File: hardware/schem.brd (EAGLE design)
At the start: 46 x 47 mm, 18 parts, among them IC1 7805L, IC2 L298

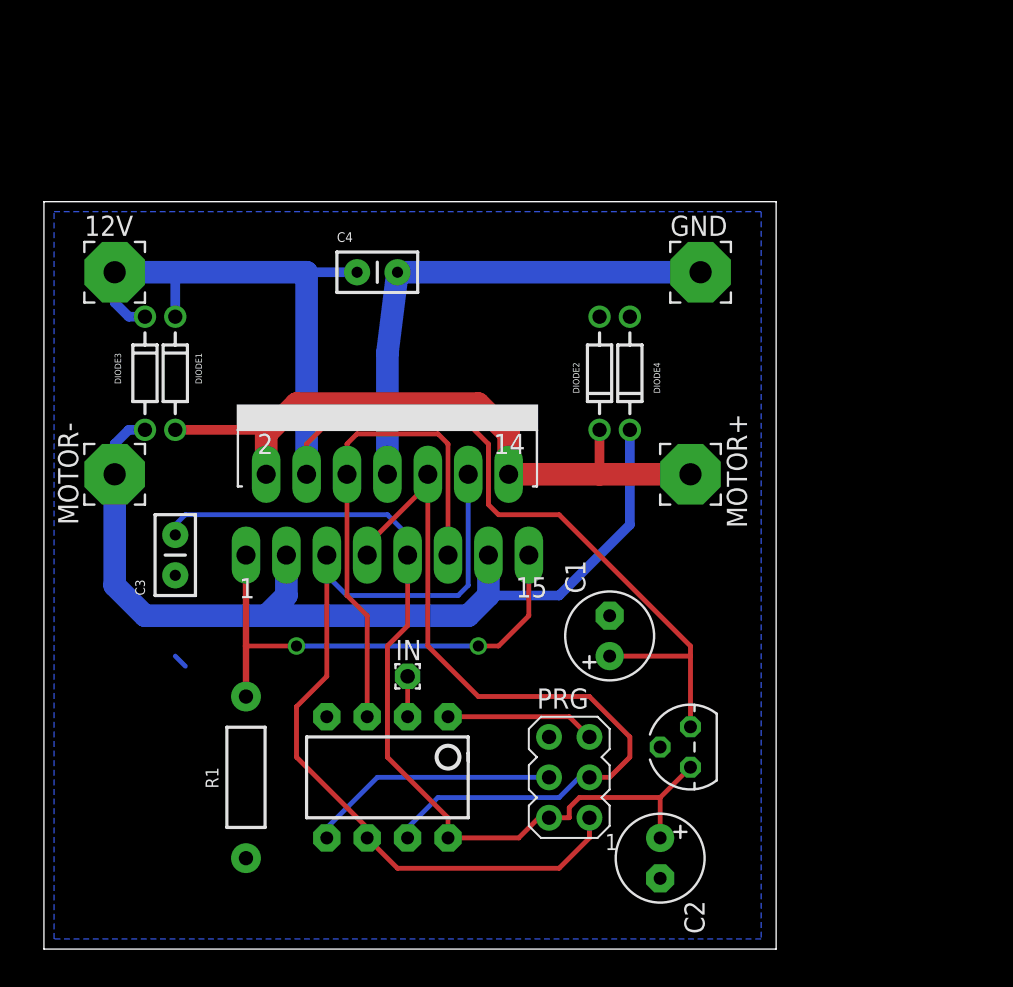
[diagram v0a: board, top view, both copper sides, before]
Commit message: added current sensing
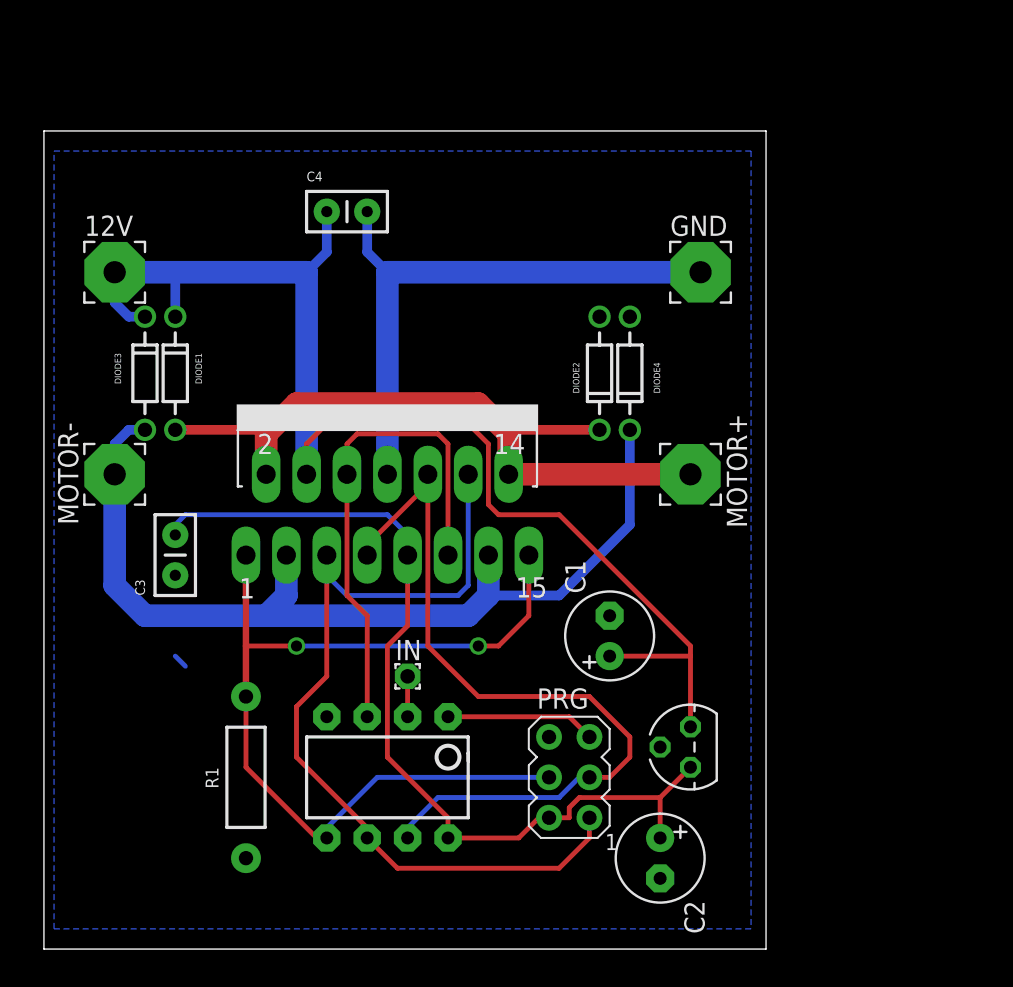
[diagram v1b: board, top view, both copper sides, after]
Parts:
- moved C4 4.26 mm to (17.8, 46.4)
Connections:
- removed net N$1: IC2.1, IC2.15, R1.P$1
- net MOSI: now also IC2.1, IC2.15, R1.P$1
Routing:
- net MOSI: track 15.9 -> 58.6 mm, vias 0 -> 2
- net N$1: track 31.3 -> 0.00 mm, vias 2 -> 0
- net GND: track 32.7 -> 37.6 mm
- net OUT1: track 42.3 -> 45.0 mm
- net +12V: track 79.7 -> 80.8 mm
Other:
- board size 46 x 47 mm -> 45.4 x 51.4 mm
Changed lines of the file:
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@@
 <board>
 <plain>
-<wire x1="0" y1="0" x2="46.025" y2="0" width="0" layer="20"/>
-<wire x1="46.025" y1="0" x2="46.025" y2="46.98" width="0" layer="20"/>
-<wire x1="46.025" y1="46.98" x2="0" y2="46.98" width="0" layer="20"/>
-<wire x1="0" y1="46.98" x2="0" y2="0" width="0" layer="20"/>
+<wire x1="0" y1="0" x2="45.39" y2="0" width="0" layer="20"/>
+<wire x1="45.39" y1="0" x2="45.39" y2="51.425" width="0" layer="20"/>
+<wire x1="45.39" y1="51.425" x2="0" y2="51.425" width="0" layer="20"/>
+<wire x1="0" y1="51.425" x2="0" y2="0" width="0" layer="20"/>
 </plain>
 <attributes>
@@
 </element>
 <element name="C3" library="SparkFun-Capacitors" package="CAP-PTH-SMALL2" value="100nF" x="8.255" y="23.495" rot="R90"/>
-<element name="C4" library="SparkFun-Capacitors" package="CAP-PTH-SMALL2" value="100nF" x="19.685" y="42.545"/>
+<element name="C4" library="SparkFun-Capacitors" package="CAP-PTH-SMALL2" value="100nF" x="17.78" y="46.355"/>
 <element name="R1" library="SparkFun-Passives" package="AXIAL-0.4" value="" x="12.7" y="10.795" smashed="yes" rot="R270">
 <attribute name="NAME" x="10.16" y="11.43" size="0.8128" layer="25" font="vector" ratio="15" rot="R270"/>
@@
 <wire x1="8.255" y1="42.545" x2="16.51" y2="42.545" width="1.4224" layer="16"/>
 <wire x1="16.51" y1="42.545" x2="16.51" y2="29.845" width="1.4224" layer="16"/>
-<wire x1="19.685" y1="42.545" x2="16.51" y2="42.545" width="0.6096" layer="16"/>
+<wire x1="17.78" y1="46.355" x2="17.78" y2="43.815" width="0.6096" layer="16"/>
+<wire x1="17.78" y1="43.815" x2="16.51" y2="42.545" width="0.6096" layer="16"/>
 <wire x1="32.385" y1="27.305" x2="28.575" y2="27.305" width="0.3048" layer="1"/>
 <wire x1="28.575" y1="27.305" x2="27.94" y2="27.94" width="0.3048" layer="1"/>
@@
 <contactref element="DIODE4" pad="P$2"/>
 <contactref element="DIODE2" pad="P$2"/>
-<wire x1="21.59" y1="29.845" x2="21.59" y2="37.465" width="1.4224" layer="16"/>
-<wire x1="21.59" y1="37.465" x2="22.225" y2="42.545" width="1.4224" layer="16"/>
-<wire x1="22.225" y1="42.545" x2="41.275" y2="42.545" width="1.4224" layer="16"/>
+<wire x1="21.59" y1="29.845" x2="21.59" y2="42.545" width="1.4224" layer="16"/>
+<wire x1="21.59" y1="42.545" x2="41.275" y2="42.545" width="1.4224" layer="16"/>
+<wire x1="20.32" y1="46.355" x2="20.32" y2="43.815" width="0.6096" layer="16"/>
+<wire x1="20.32" y1="43.815" x2="21.59" y2="42.545" width="0.6096" layer="16"/>
 <polygon width="0.3048" layer="16" isolate="0.6096">
-<vertex x="0.635" y="46.355"/>
-<vertex x="45.085" y="46.355"/>
-<vertex x="45.085" y="0.635"/>
-<vertex x="0.635" y="0.635"/>
+<vertex x="0.635" y="50.165"/>
+<vertex x="44.45" y="50.165"/>
+<vertex x="44.45" y="1.27"/>
+<vertex x="0.635" y="1.27"/>
 </polygon>
 <wire x1="8.255" y1="18.415" x2="8.89" y2="17.78" width="0.3048" layer="16"/>
@@
 <wire x1="20.955" y1="10.795" x2="17.78" y2="7.62" width="0.3048" layer="16"/>
 <wire x1="17.78" y1="7.62" x2="17.78" y2="6.985" width="0.3048" layer="16"/>
+<contactref element="IC2" pad="1"/>
+<contactref element="IC2" pad="15"/>
+<contactref element="R1" pad="P$1"/>
+<wire x1="12.7" y1="24.765" x2="12.7" y2="19.05" width="0.4064" layer="1"/>
+<wire x1="12.7" y1="19.05" x2="12.7" y2="15.875" width="0.4064" layer="1"/>
+<wire x1="30.48" y1="24.765" x2="30.48" y2="20.955" width="0.3048" layer="1"/>
+<wire x1="30.48" y1="20.955" x2="28.575" y2="19.05" width="0.3048" layer="1"/>
+<via x="27.305" y="19.05" extent="1-16" drill="0.7"/>
+<wire x1="27.305" y1="19.05" x2="15.875" y2="19.05" width="0.3048" layer="16"/>
+<via x="15.875" y="19.05" extent="1-16" drill="0.7"/>
+<wire x1="15.875" y1="19.05" x2="12.7" y2="19.05" width="0.3048" layer="1"/>
+<wire x1="28.575" y1="19.05" x2="27.305" y2="19.05" width="0.3048" layer="1"/>
+<wire x1="17.78" y1="6.985" x2="17.145" y2="6.985" width="0.3048" layer="1"/>
+<wire x1="17.145" y1="6.985" x2="12.7" y2="11.43" width="0.3048" layer="1"/>
+<wire x1="12.7" y1="11.43" x2="12.7" y2="15.875" width="0.3048" layer="1"/>
 </signal>
 <signal name="MISO">
@@
 <contactref element="DIODE2" pad="P$1"/>
 <contactref element="DIODE1" pad="P$2"/>
-<wire x1="40.64" y1="29.845" x2="34.925" y2="29.845" width="1.4224" layer="1"/>
-<wire x1="34.925" y1="29.845" x2="29.21" y2="29.845" width="1.4224" layer="1"/>
+<wire x1="40.64" y1="29.845" x2="29.21" y2="29.845" width="1.4224" layer="1"/>
 <wire x1="13.97" y1="29.845" x2="13.97" y2="32.385" width="1.4224" layer="1"/>
 <wire x1="13.97" y1="32.385" x2="15.875" y2="34.29" width="1.4224" layer="1"/>
@@
 <wire x1="8.255" y1="32.639" x2="13.716" y2="32.639" width="0.6096" layer="1"/>
 <wire x1="13.716" y1="32.639" x2="13.97" y2="32.385" width="0.6096" layer="1"/>
+<wire x1="34.925" y1="32.639" x2="29.464" y2="32.639" width="0.6096" layer="1"/>
 <wire x1="29.464" y1="32.639" x2="29.21" y2="32.385" width="0.6096" layer="1"/>
-<wire x1="34.925" y1="32.639" x2="34.925" y2="29.845" width="0.6096" layer="1"/>
-</signal>
-<signal name="N$1">
-<contactref element="IC2" pad="1"/>
-<contactref element="IC2" pad="15"/>
-<contactref element="R1" pad="P$1"/>
-<wire x1="12.7" y1="24.765" x2="12.7" y2="19.05" width="0.4064" layer="1"/>
-<wire x1="12.7" y1="19.05" x2="12.7" y2="15.875" width="0.4064" layer="1"/>
-<wire x1="30.48" y1="24.765" x2="30.48" y2="20.955" width="0.3048" layer="1"/>
-<wire x1="30.48" y1="20.955" x2="28.575" y2="19.05" width="0.3048" layer="1"/>
-<wire x1="28.575" y1="19.05" x2="27.305" y2="19.05" width="0.3048" layer="1"/>
-<via x="27.305" y="19.05" extent="1-16" drill="0.7"/>
-<wire x1="27.305" y1="19.05" x2="15.875" y2="19.05" width="0.3048" layer="16"/>
-<via x="15.875" y="19.05" extent="1-16" drill="0.7"/>
-<wire x1="15.875" y1="19.05" x2="12.7" y2="19.05" width="0.3048" layer="1"/>
 </signal>
 <signal name="ENA">

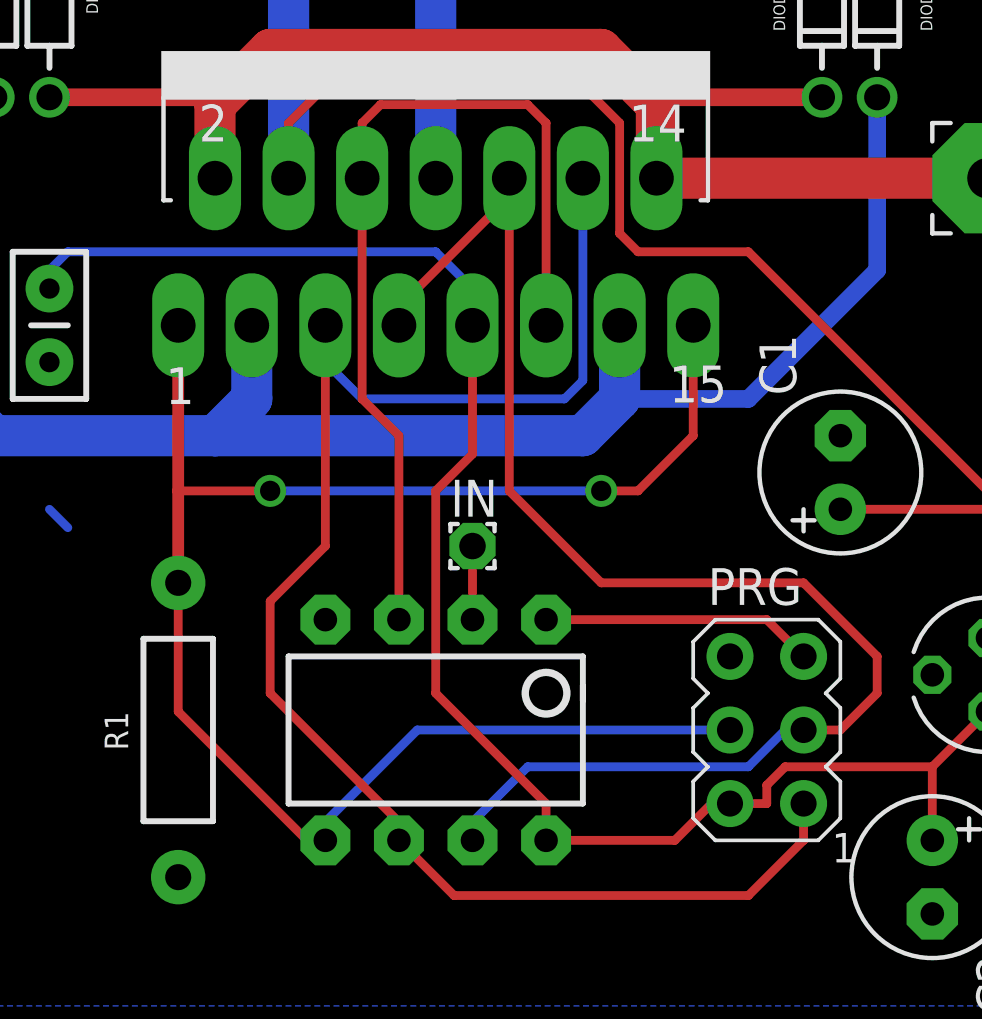
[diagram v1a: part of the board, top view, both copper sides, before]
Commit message: Changed Current Sense pin
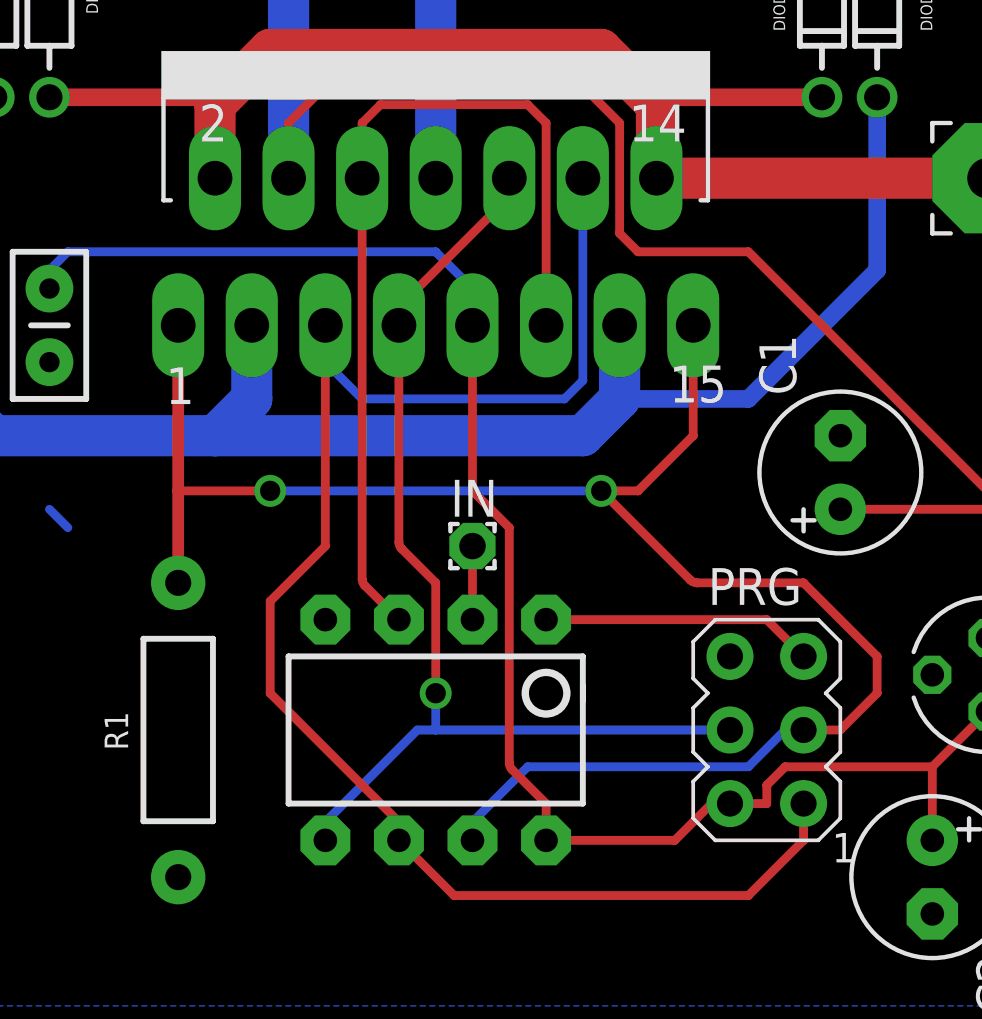
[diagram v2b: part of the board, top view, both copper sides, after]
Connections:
- net MOSI: now also IC2.10, IC2.7; no longer IC2.1, IC2.15, R1.P$1
- net SCK: now also IC2.1, IC2.15, R1.P$1; no longer IC2.10, IC2.7
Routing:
- net MOSI: track 58.6 -> 37.0 mm, vias 2 -> 1
- net SCK: track 49.6 -> 60.9 mm, vias 0 -> 2
- net +5V: track 57.2 -> 56.1 mm
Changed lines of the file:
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@@
 <wire x1="31.115" y1="8.255" x2="29.845" y2="6.985" width="0.3048" layer="1"/>
 <wire x1="29.845" y1="6.985" x2="25.4" y2="6.985" width="0.3048" layer="1"/>
-<wire x1="22.86" y1="24.765" x2="22.86" y2="20.32" width="0.3048" layer="1"/>
+<wire x1="22.86" y1="24.765" x2="22.86" y2="19.1815125" width="0.3048" layer="1"/>
 <wire x1="25.4" y1="8.255" x2="25.4" y2="6.985" width="0.3048" layer="1"/>
-<wire x1="22.86" y1="20.32" x2="21.59" y2="19.05" width="0.3048" layer="1"/>
-<wire x1="21.59" y1="19.05" x2="21.59" y2="12.065" width="0.3048" layer="1"/>
-<wire x1="21.59" y1="12.065" x2="25.4" y2="8.255" width="0.3048" layer="1"/>
 <wire x1="38.735" y1="9.525" x2="40.64" y2="11.43" width="0.3048" layer="1"/>
 <wire x1="38.735" y1="6.985" x2="38.735" y2="9.525" width="0.3048" layer="1"/>
@@
 <wire x1="8.255" y1="26.67" x2="8.89" y2="27.305" width="0.3048" layer="16"/>
 <wire x1="8.89" y1="27.305" x2="21.59" y2="27.305" width="0.3048" layer="16"/>
+<wire x1="22.86" y1="19.1815125" x2="22.95299375" y2="18.95700625" width="0.3048" layer="1" curve="45"/>
+<wire x1="22.95299375" y1="18.95700625" x2="24.13" y2="17.78" width="0.3048" layer="1"/>
+<wire x1="24.13" y1="17.78" x2="24.13" y2="9.6565125" width="0.3048" layer="1"/>
+<wire x1="24.13" y1="9.6565125" x2="24.22299375" y2="9.43200625" width="0.3048" layer="1" curve="45"/>
+<wire x1="24.22299375" y1="9.43200625" x2="25.4" y2="8.255" width="0.3048" layer="1"/>
 </signal>
 <signal name="INP">
@@
 <contactref element="PRG" pad="4"/>
 <contactref element="TINY85" pad="5"/>
-<wire x1="31.75" y1="10.795" x2="20.955" y2="10.795" width="0.3048" layer="16"/>
+<wire x1="31.75" y1="10.795" x2="21.59" y2="10.795" width="0.3048" layer="16"/>
+<wire x1="21.59" y1="10.795" x2="20.955" y2="10.795" width="0.3048" layer="16"/>
 <wire x1="20.955" y1="10.795" x2="17.78" y2="7.62" width="0.3048" layer="16"/>
 <wire x1="17.78" y1="7.62" x2="17.78" y2="6.985" width="0.3048" layer="16"/>
-<contactref element="IC2" pad="1"/>
-<contactref element="IC2" pad="15"/>
-<contactref element="R1" pad="P$1"/>
-<wire x1="12.7" y1="24.765" x2="12.7" y2="19.05" width="0.4064" layer="1"/>
-<wire x1="12.7" y1="19.05" x2="12.7" y2="15.875" width="0.4064" layer="1"/>
-<wire x1="30.48" y1="24.765" x2="30.48" y2="20.955" width="0.3048" layer="1"/>
-<wire x1="30.48" y1="20.955" x2="28.575" y2="19.05" width="0.3048" layer="1"/>
-<via x="27.305" y="19.05" extent="1-16" drill="0.7"/>
-<wire x1="27.305" y1="19.05" x2="15.875" y2="19.05" width="0.3048" layer="16"/>
-<via x="15.875" y="19.05" extent="1-16" drill="0.7"/>
-<wire x1="15.875" y1="19.05" x2="12.7" y2="19.05" width="0.3048" layer="1"/>
-<wire x1="28.575" y1="19.05" x2="27.305" y2="19.05" width="0.3048" layer="1"/>
-<wire x1="17.78" y1="6.985" x2="17.145" y2="6.985" width="0.3048" layer="1"/>
-<wire x1="17.145" y1="6.985" x2="12.7" y2="11.43" width="0.3048" layer="1"/>
-<wire x1="12.7" y1="11.43" x2="12.7" y2="15.875" width="0.3048" layer="1"/>
+<contactref element="IC2" pad="10"/>
+<contactref element="IC2" pad="7"/>
+<wire x1="24.13" y1="29.845" x2="24.13" y2="29.3415125" width="0.3048" layer="1"/>
+<wire x1="24.13" y1="29.3415125" x2="24.03700625" y2="29.11700625" width="0.3048" layer="1" curve="-45"/>
+<wire x1="24.03700625" y1="29.11700625" x2="20.32" y2="25.4" width="0.3048" layer="1"/>
+<wire x1="20.32" y1="25.4" x2="20.32" y2="24.765" width="0.3048" layer="1"/>
+<wire x1="20.32" y1="24.765" x2="20.32" y2="17.2765125" width="0.3048" layer="1"/>
+<wire x1="20.32" y1="17.2765125" x2="20.41299375" y2="17.05200625" width="0.3048" layer="1" curve="45"/>
+<wire x1="20.41299375" y1="17.05200625" x2="21.59" y2="15.875" width="0.3048" layer="1"/>
+<wire x1="21.59" y1="15.875" x2="21.59" y2="12.065" width="0.3048" layer="1"/>
+<via x="21.59" y="12.065" extent="1-16" drill="0.7" diameter="0.8128"/>
+<wire x1="21.59" y1="12.065" x2="21.59" y2="10.795" width="0.3048" layer="16"/>
 </signal>
 <signal name="MISO">
@@
 <wire x1="24.765" y1="9.525" x2="22.86" y2="7.62" width="0.3048" layer="16"/>
 <wire x1="22.86" y1="7.62" x2="22.86" y2="6.985" width="0.3048" layer="16"/>
-<wire x1="24.13" y1="19.05" x2="27.305" y2="15.875" width="0.3048" layer="1"/>
-<wire x1="27.305" y1="15.875" x2="34.29" y2="15.875" width="0.3048" layer="1"/>
 <wire x1="34.29" y1="15.875" x2="36.83" y2="13.335" width="0.3048" layer="1"/>
 <wire x1="36.83" y1="13.335" x2="36.83" y2="12.065" width="0.3048" layer="1"/>
 <wire x1="36.83" y1="12.065" x2="35.56" y2="10.795" width="0.3048" layer="1"/>
 <wire x1="35.56" y1="10.795" x2="34.29" y2="10.795" width="0.3048" layer="1"/>
-<contactref element="IC2" pad="10"/>
-<contactref element="IC2" pad="7"/>
-<wire x1="20.32" y1="24.765" x2="20.32" y2="25.4" width="0.3048" layer="1"/>
-<wire x1="20.32" y1="25.4" x2="24.13" y2="29.21" width="0.3048" layer="1"/>
-<wire x1="24.13" y1="29.21" x2="24.13" y2="29.845" width="0.3048" layer="1"/>
-<wire x1="24.13" y1="19.05" x2="24.13" y2="29.21" width="0.3048" layer="1"/>
+<contactref element="IC2" pad="1"/>
+<contactref element="IC2" pad="15"/>
+<contactref element="R1" pad="P$1"/>
+<wire x1="12.7" y1="24.765" x2="12.7" y2="19.05" width="0.4064" layer="1"/>
+<wire x1="12.7" y1="19.05" x2="12.7" y2="15.875" width="0.4064" layer="1"/>
+<wire x1="30.48" y1="24.765" x2="30.48" y2="20.955" width="0.3048" layer="1"/>
+<wire x1="30.48" y1="20.955" x2="28.575" y2="19.05" width="0.3048" layer="1"/>
+<via x="27.305" y="19.05" extent="1-16" drill="0.7"/>
+<wire x1="27.305" y1="19.05" x2="15.875" y2="19.05" width="0.3048" layer="16"/>
+<via x="15.875" y="19.05" extent="1-16" drill="0.7"/>
+<wire x1="15.875" y1="19.05" x2="12.7" y2="19.05" width="0.3048" layer="1"/>
+<wire x1="28.575" y1="19.05" x2="27.305" y2="19.05" width="0.3048" layer="1"/>
+<wire x1="34.29" y1="15.875" x2="30.6115125" y2="15.875" width="0.3048" layer="1"/>
+<wire x1="30.6115125" y1="15.875" x2="30.38700625" y2="15.96799375" width="0.3048" layer="1" curve="-45"/>
+<wire x1="30.38700625" y1="15.96799375" x2="27.305" y2="19.05" width="0.3048" layer="1"/>
 </signal>
 <signal name="OUT2">
@@
 <wire x1="19.05" y1="31.75" x2="19.05" y2="29.845" width="0.3048" layer="1"/>
 <contactref element="TINY85" pad="3"/>
-<wire x1="20.32" y1="14.605" x2="20.32" y2="20.955" width="0.3048" layer="1"/>
-<wire x1="20.32" y1="20.955" x2="19.05" y2="22.225" width="0.3048" layer="1"/>
-<wire x1="19.05" y1="22.225" x2="19.05" y2="29.845" width="0.3048" layer="1"/>
+<wire x1="19.05" y1="16.0065125" x2="19.05" y2="29.845" width="0.3048" layer="1"/>
+<wire x1="19.05" y1="16.0065125" x2="19.14299375" y2="15.78200625" width="0.3048" layer="1" curve="45"/>
+<wire x1="19.14299375" y1="15.78200625" x2="20.32" y2="14.605" width="0.3048" layer="1"/>
 </signal>
 </signals>
